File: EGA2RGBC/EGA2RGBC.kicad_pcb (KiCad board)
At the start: 2 copper layers, 26 parts, among them J1 EGA Input, J2 CGA/EGA Selection, J3 CSync Selection, J4 Power, J5 Video Out, U1 74LS244, U2 74LS138, U3 74LS86

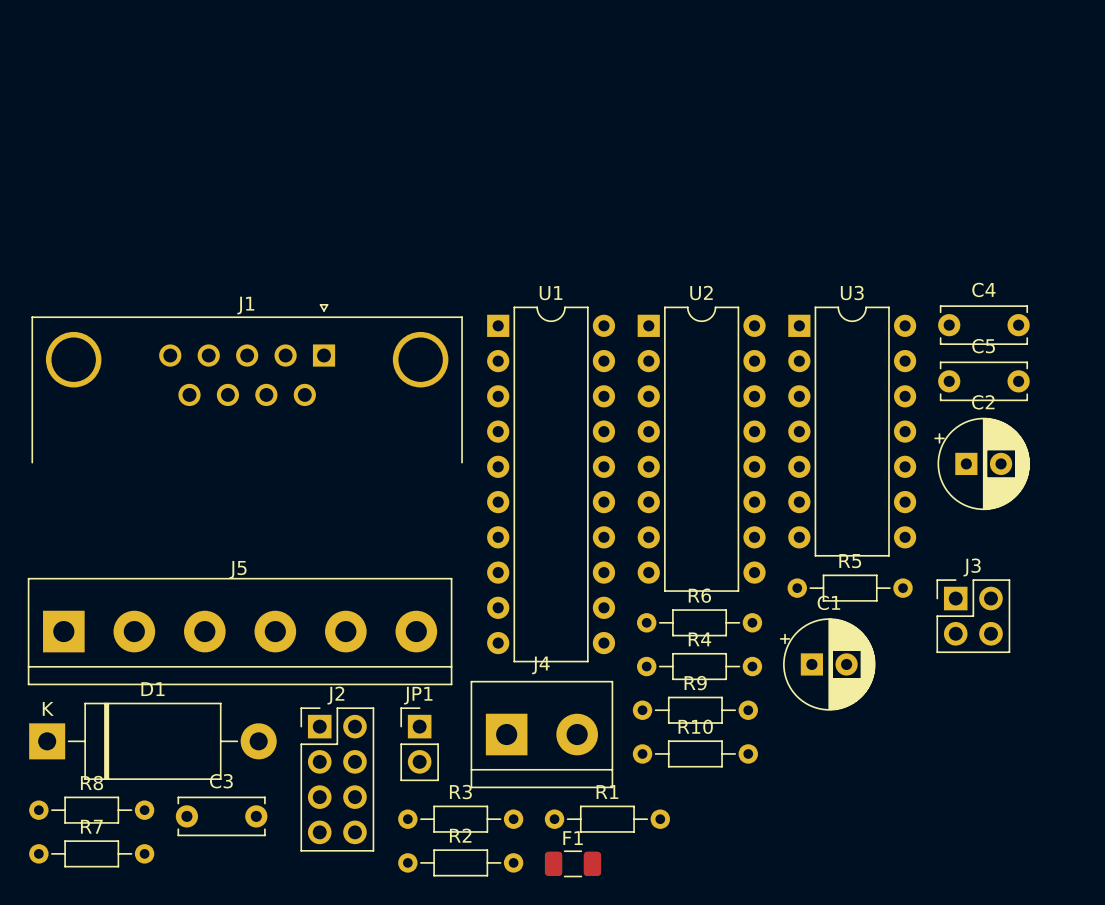
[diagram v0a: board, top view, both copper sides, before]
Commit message: Fix labels and generate gerbers
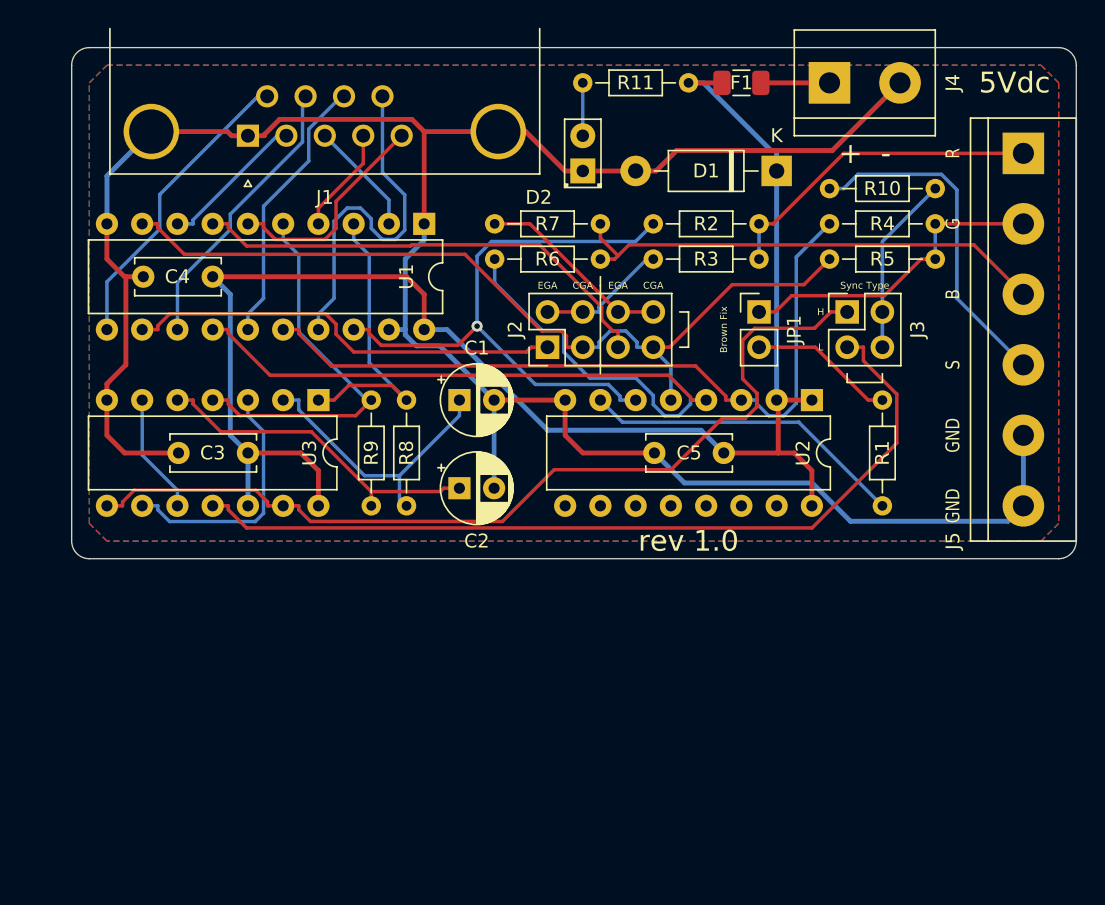
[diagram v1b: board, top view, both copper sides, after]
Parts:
- added D2: Power, LED_THT:LED_D2.0mm_W4.8mm_H2.5mm_FlatTop, F.Cu at (125.7, 44.5)
- added R11: 1k, Resistor_THT:R_Axial_DIN0204_L3.6mm_D1.6mm_P7.62mm_Horizontal, F.Cu at (125.7, 38.1)
- C1, C2: footprint Capacitor_THT:CP_Radial_D6.3mm_P2.50mm -> Capacitor_THT:CP_Radial_D5.0mm_P2.50mm
- D1: value 1N5338B -> 1N4733A; footprint Diode_THT:D_DO-201_P15.24mm_Horizontal -> Diode_THT:D_DO-41_SOD81_P10.16mm_Horizontal
- moved J5 77.3 mm to (157.5, 43.2), turned to 270 degrees
- moved D1 66.7 mm to (139.7, 44.5), turned to 180 degrees
- moved F1 57.6 mm to (137.2, 38.1)
- moved R7 56.0 mm to (119.4, 48.3)
- moved C4 53.2 mm to (99.1, 52.1), turned to 180 degrees
- moved J4 52.4 mm to (143.5, 38.1)
- moved R2 49.3 mm to (130.8, 48.3)
- moved R10 45.9 mm to (151.1, 45.7), turned to 180 degrees
- moved R3 44.1 mm to (130.8, 50.8)
- moved R8 39.7 mm to (113.0, 61.0), turned to 270 degrees
- moved JP1 38.6 mm to (138.4, 54.6)
- moved C2 36.6 mm to (116.8, 67.3)
- moved U3 35.1 mm to (106.7, 61.0), turned to 270 degrees
- moved R4 34.5 mm to (143.5, 48.3)
- moved R1 32.7 mm to (147.3, 68.6), turned to 90 degrees
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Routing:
- net GND: track 0.00 -> 170.0 mm
- net VCC: track 0.00 -> 113.8 mm
- net /C_SYNC_TTL: track 0.00 -> 65.8 mm
- net /BUF_G_I: track 0.00 -> 62.3 mm
- net /~C_SYNC_TTL: track 0.00 -> 61.7 mm
- net /BUF_B: track 0.00 -> 60.7 mm
- net /BUF_G: track 0.00 -> 54.3 mm
- net /BUF_R: track 0.00 -> 42.6 mm, vias 0 -> 1
- net /ANALOG_B: track 0.00 -> 35.2 mm
- net /BUF_B_I: track 0.00 -> 34.3 mm
- net /BUF_R_I: track 0.00 -> 31.5 mm
- net /BUF_HS: track 0.00 -> 28.0 mm
- net /IN_VS: track 0.00 -> 25.7 mm
- net /ANALOG_CSYNC: track 0.00 -> 24.7 mm
- net Net-(C2-Pad1): track 0.00 -> 24.3 mm
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- added copper zone on B.Cu, net GND
- added copper zone on F.Cu, net GND
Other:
- board outline added: 72.4 x 36.8 mm
- net class Power added: clearance 0.2, trace_width 0.35, via_dia 0.8, via_drill 0.4
- board text added: "+ -"
- board text added: "5Vdc"
- board text added: "B"
- board text added: "Brown Fix"
- board text added: "CGA"
- board text added: "EGA"
- board text added: "EGA-2-RGBS"
- board text added: "G"
- board text added: "GND"
- board text added: "H"
- board text added: "L"
- board text added: "R"
- board text added: "S"
- board text added: "Sync Type"
- board text added: "rev 1.0"
